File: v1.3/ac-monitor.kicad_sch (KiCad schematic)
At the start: 5 parts, among them U5 MID400

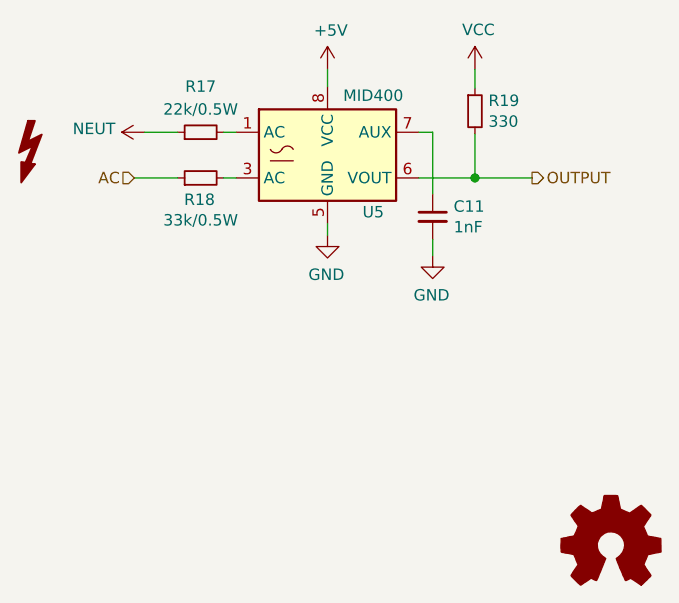
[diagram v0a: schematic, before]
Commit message: Change TRIAC type in schematics
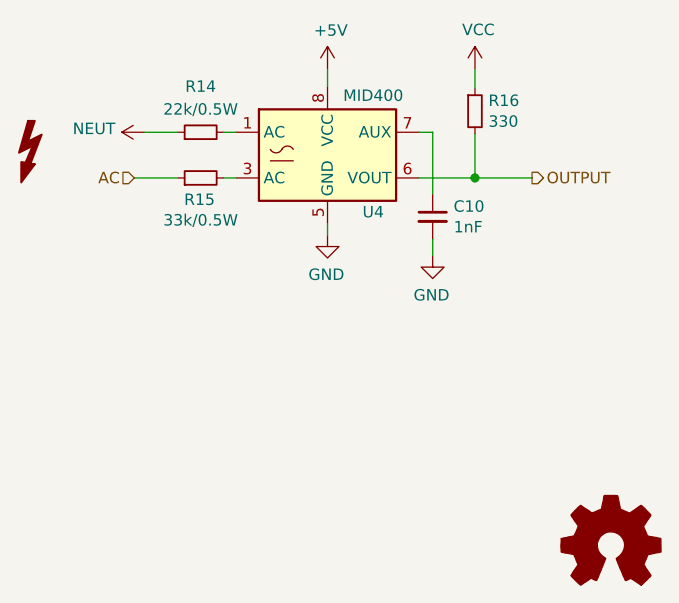
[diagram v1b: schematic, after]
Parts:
- renumbered C11 to C10, R17 to R14, R18 to R15, R19 to R16, U5 to U4
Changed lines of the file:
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@@
   (symbol (lib_id "power:NEUT") (at 83.82 66.04 90)
     (in_bom yes) (on_board yes)
-    (property "Reference" "#PWR040" (id 0) (at 87.63 66.04 0)
+    (property "Reference" "#PWR035" (id 0) (at 87.63 66.04 0)
       (effects (font (size 1.27 1.27)) hide)
     )
@@
   (symbol (lib_id "power:+5V") (at 104.14 59.055 0)
     (in_bom yes) (on_board yes)
-    (property "Reference" "#PWR041" (id 0) (at 104.14 62.865 0)
+    (property "Reference" "#PWR036" (id 0) (at 104.14 62.865 0)
       (effects (font (size 1.27 1.27)) hide)
     )
@@
   (symbol (lib_id "power:VCC") (at 120.523 59.055 0)
     (in_bom yes) (on_board yes)
-    (property "Reference" "#PWR044" (id 0) (at 120.523 62.865 0)
+    (property "Reference" "#PWR039" (id 0) (at 120.523 62.865 0)
       (effects (font (size 1.27 1.27)) hide)
     )
@@
   (symbol (lib_id "power:GND") (at 104.14 77.47 0) (mirror y)
     (in_bom yes) (on_board yes)
-    (property "Reference" "#PWR042" (id 0) (at 104.14 83.82 0)
+    (property "Reference" "#PWR037" (id 0) (at 104.14 83.82 0)
       (effects (font (size 1.27 1.27)) hide)
     )
@@
   (symbol (lib_id "power:GND") (at 115.824 79.756 0) (mirror y)
     (in_bom yes) (on_board yes)
-    (property "Reference" "#PWR043" (id 0) (at 115.824 86.106 0)
+    (property "Reference" "#PWR038" (id 0) (at 115.824 86.106 0)
       (effects (font (size 1.27 1.27)) hide)
     )
@@
   (symbol (lib_id "Device:R_Small") (at 90.043 66.04 90)
     (in_bom yes) (on_board yes)
-    (property "Reference" "R17" (id 0) (at 90.043 60.96 90))
+    (property "Reference" "R14" (id 0) (at 90.043 60.96 90))
     (property "Value" "22k/0.5W" (id 1) (at 90.043 63.5 90))
     (property "Footprint" "Resistor_SMD:R_1206_3216Metric_Pad1.30x1.75mm_HandSolder" (id 2) (at 90.043 66.04 0)
@@
   (symbol (lib_id "Device:R_Small") (at 90.043 71.12 90)
     (in_bom yes) (on_board yes)
-    (property "Reference" "R18" (id 0) (at 89.916 73.533 90))
+    (property "Reference" "R15" (id 0) (at 89.916 73.533 90))
     (property "Value" "33k/0.5W" (id 1) (at 90.043 75.819 90))
     (property "Footprint" "Resistor_SMD:R_1206_3216Metric_Pad1.30x1.75mm_HandSolder" (id 2) (at 90.043 71.12 0)
@@
   (symbol (lib_id "Device:R_Small") (at 120.523 63.7032 0)
     (in_bom yes) (on_board yes)
-    (property "Reference" "R19" (id 0) (at 122.0216 62.5348 0)
+    (property "Reference" "R16" (id 0) (at 122.0216 62.5348 0)
       (effects (font (size 1.27 1.27)) (justify left))
     )
@@
   (symbol (lib_id "Device:C_Small") (at 115.824 75.438 0)
     (in_bom yes) (on_board yes)
-    (property "Reference" "C11" (id 0) (at 118.1482 74.2886 0)
+    (property "Reference" "C10" (id 0) (at 118.1482 74.2886 0)
       (effects (font (size 1.27 1.27)) (justify left))
     )
@@
   (symbol (lib_id "Isolator:MID400") (at 104.14 68.58 0)
     (in_bom yes) (on_board yes)
-    (property "Reference" "U5" (id 0) (at 109.22 74.9108 0))
+    (property "Reference" "U4" (id 0) (at 109.22 74.9108 0))
     (property "Value" "MID400" (id 1) (at 109.22 61.9695 0))
     (property "Footprint" "Package_DIP:SMDIP-8_W9.53mm" (id 2) (at 104.14 68.58 0)
